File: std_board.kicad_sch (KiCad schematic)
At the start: 208 parts, among them IC1 ESP32, IC2 ACS712, IC4 AMS1117-V, J1 Jumper, J10 J_DHT11, J11 Jumper, J12 Jumper, J14 Jumper, J15 Jumper, J16 J_PRess, J17 Jumper, J18 Jumper, J19 Jumper, J2 Jumper, J20 Jumper, J21 Jumper, J22 Jumper, J23 Jumper, J24 Jumper, J25 Jumper, J26 Jumper, J3 Jumper, J31 Jumper, J32 Jumper, J33 Jumper, J34 Jumper, J35 Jumper, J36 Jumper, J37 Jumper, J38 Jumper, J39 Jumper, J4 Jumper, J40 Jumper, J41 Jumper, J42 Jumper, J43 Jumper, J44 Jumper, J45 Jumper, J5 Jumper, J6 Jumper, J9 Jumper, T1 TRIAC_Micro, T10 TRIAC_Micro, T2 TRIAC_Micro, T3 TRIAC_Micro, T4 NPN_MMBT222A, T5 NPN_MMBT222A, T6 NPN_MMBT222A, T7 NPN_MMBT222A, T8 PNP_2N3906, T9 NPN_MMBT222A, U1 LNK306, U3 L7805CV

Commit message: board update some documentation of pinout link with description
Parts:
- removed C22: 2.2 uF, thmalmeida:C3_elec_5x4.5_pth, symbol std_board-rescue:CP_Micro-thmalmeida
- removed C23: 22 uF, thmalmeida:C3_elec_5x4.5_pth, symbol std_board-rescue:CP_Micro-thmalmeida
- removed IC4: AMS1117-V, Package_TO_SOT_SMD:SOT-223, symbol std_board-rescue:AMS1117-V-thmalmeida
- removed J35: Jumper, thmalmeida:J_0603, symbol std_board-rescue:Jumper-thmalmeida
- added C22: 47 nF, Capacitor_SMD:C_0805_2012Metric, symbol std_board-rescue:C_Micro-RESCUE-[GenericBoard]_standard_pcb-[GenericBoard]-stan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
- added R72: 56 k, Resistor_SMD:R_0805_2012Metric, symbol std_board-rescue:R_Micro-thmalmeida
- added R77, R78: 330, Resistor_SMD:R_0805_2012Metric, symbol std_board-rescue:R_Micro-thmalmeida
- J38: Spice_Model Jumper -> (none); Spice_Netlist_Enabled Y -> (none); Spice_Primitive X -> (none)
- Opto4: footprint Housings_DIP:DIP-6_W7.62mm -> Package_DIP:DIP-6_W7.62mm
- R45: value 180 k -> 39 k
- R46, R48: value 120 -> 3.3 k
- R47: value 180 k -> 56 k
- R60: value 120 k -> 39 k
- T1: footprint thmalmeida:TO-220_thm -> Package_TO_SOT_THT:TO-220-3_Vertical
- T3: footprint TO_SOT_Packages_THT:TO-220_Neutral123_Vertical -> Package_TO_SOT_THT:TO-220-3_Vertical
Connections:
- net +3.3V: now also R72.1 (A)
- net +5V: now also J42.1 (A), U3.1 (IN)
- net GND: now also C22.2 (B)
- net Power_AC_R: no longer R70.1 (A), R71.1 (A), T10.2 (A)
- net Power_AC_T: now also R70.1 (A), R71.1 (A), T10.2 (A)
- net iSensor1: now also R77.1 (A)
- net iSensor2: now also R78.1 (A)
- net at C19.1 (A), LS1.2 (B), R46.2 (B)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: now also R77.2 (B)
- net at C20.1 (A), LS2.2 (B), R48.2 (B)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: now also R78.2 (B)
- new net K0_in: C22.1 (A), R72.2 (B)
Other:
- moved on the sheet: C10, C11, C19, C20, C8, C9, F1, Inputs1, J23, J34, J36, J37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

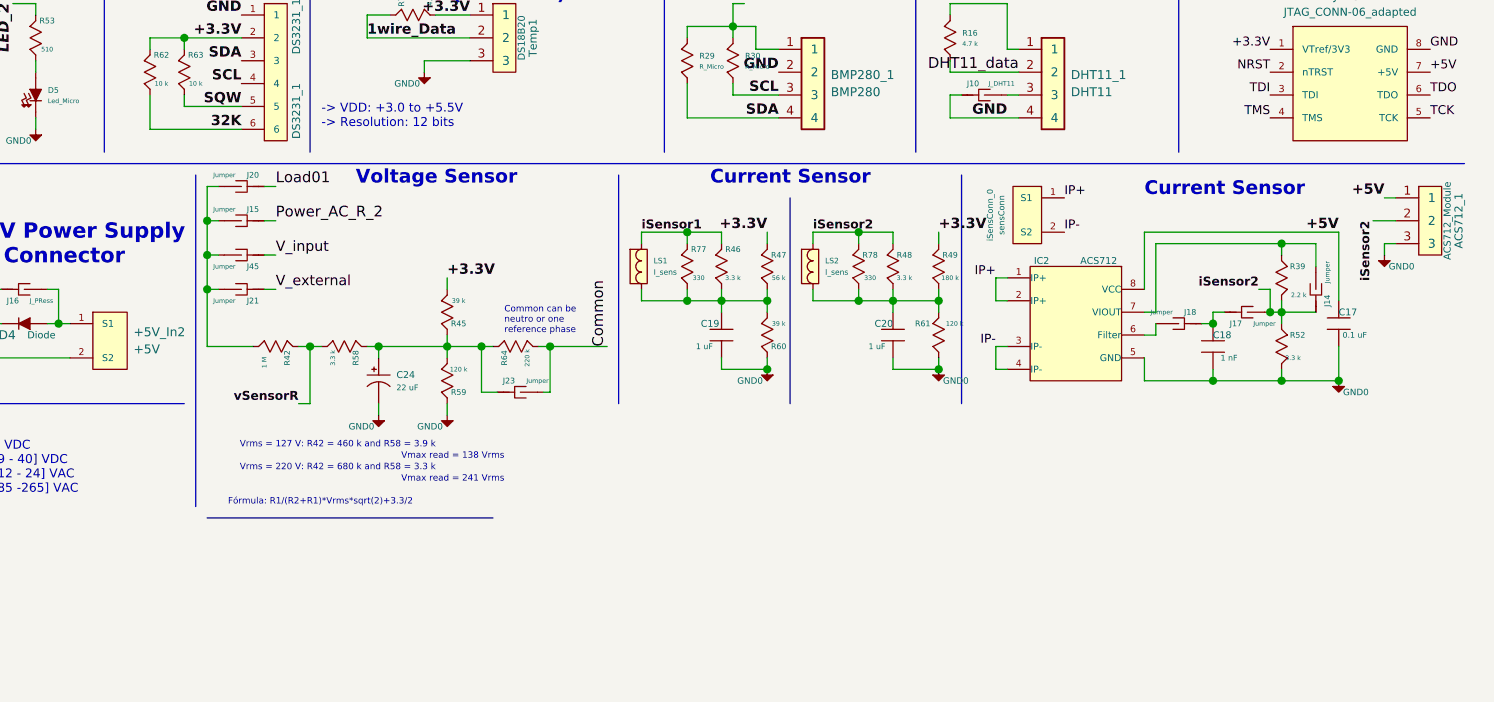
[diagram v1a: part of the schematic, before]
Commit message: current sensor 1 added resistors for voltage divider
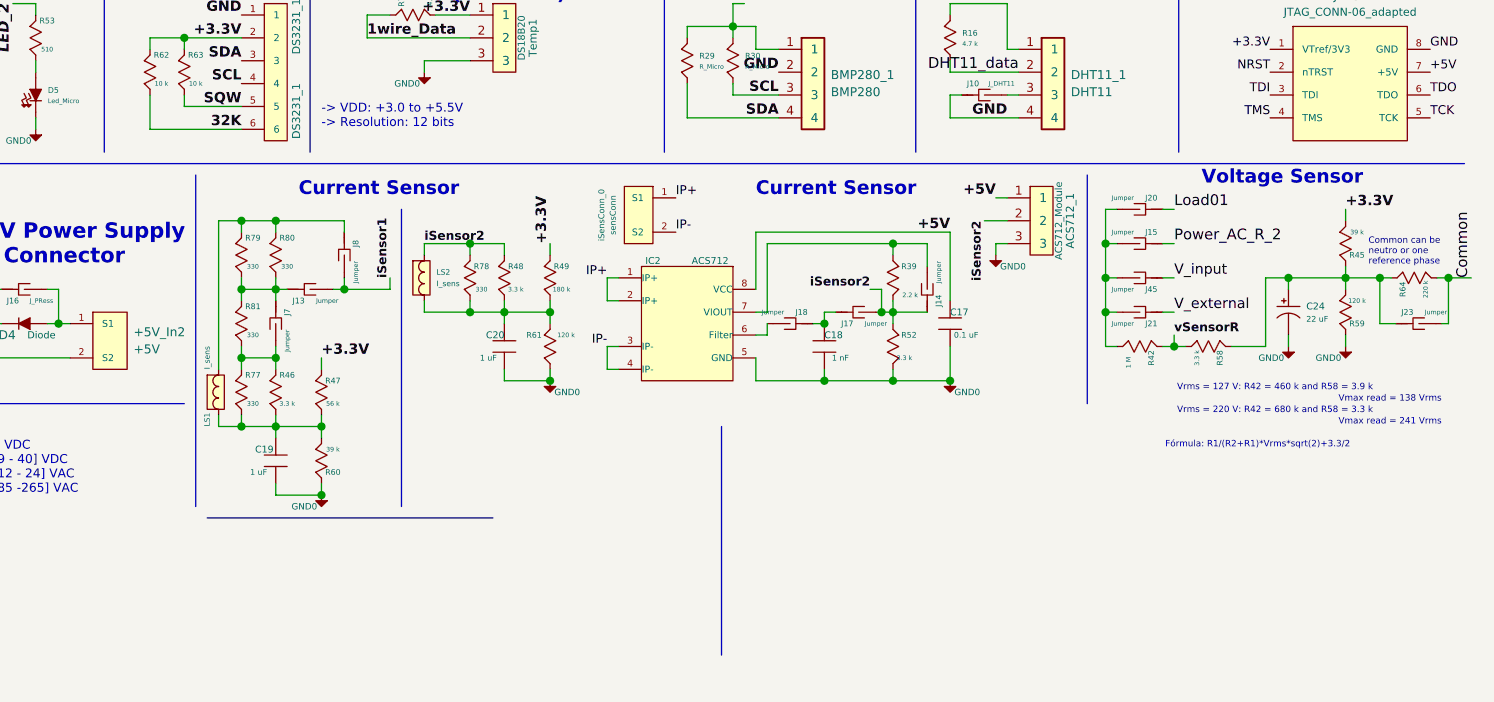
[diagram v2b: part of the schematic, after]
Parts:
- added J13, J7, J8: Jumper, thmalmeida:J_0603, symbol std_board-rescue:Jumper-thmalmeida
- added R79, R80, R81: 330, Resistor_SMD:R_0805_2012Metric, symbol std_board-rescue:R_Micro-thmalmeida
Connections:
- net iSensor1: now also J13.2 (B), J8.2 (B); no longer LS1.1 (A), R46.1 (A), R77.1 (A)
- new net: J7.2 (B), R46.1 (A), R77.1 (A), R81.2 (B)
- new net: J8.1 (A), LS1.1 (A), R79.1 (A), R80.1 (A)
- new net: J13.1 (A), J7.1 (A), R79.2 (B), R80.2 (B), R81.1 (A)
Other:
- moved on the sheet: ACS712_1, C17, C18, C19, C20, C24, IC2, J14, J15, J17, J18, J20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

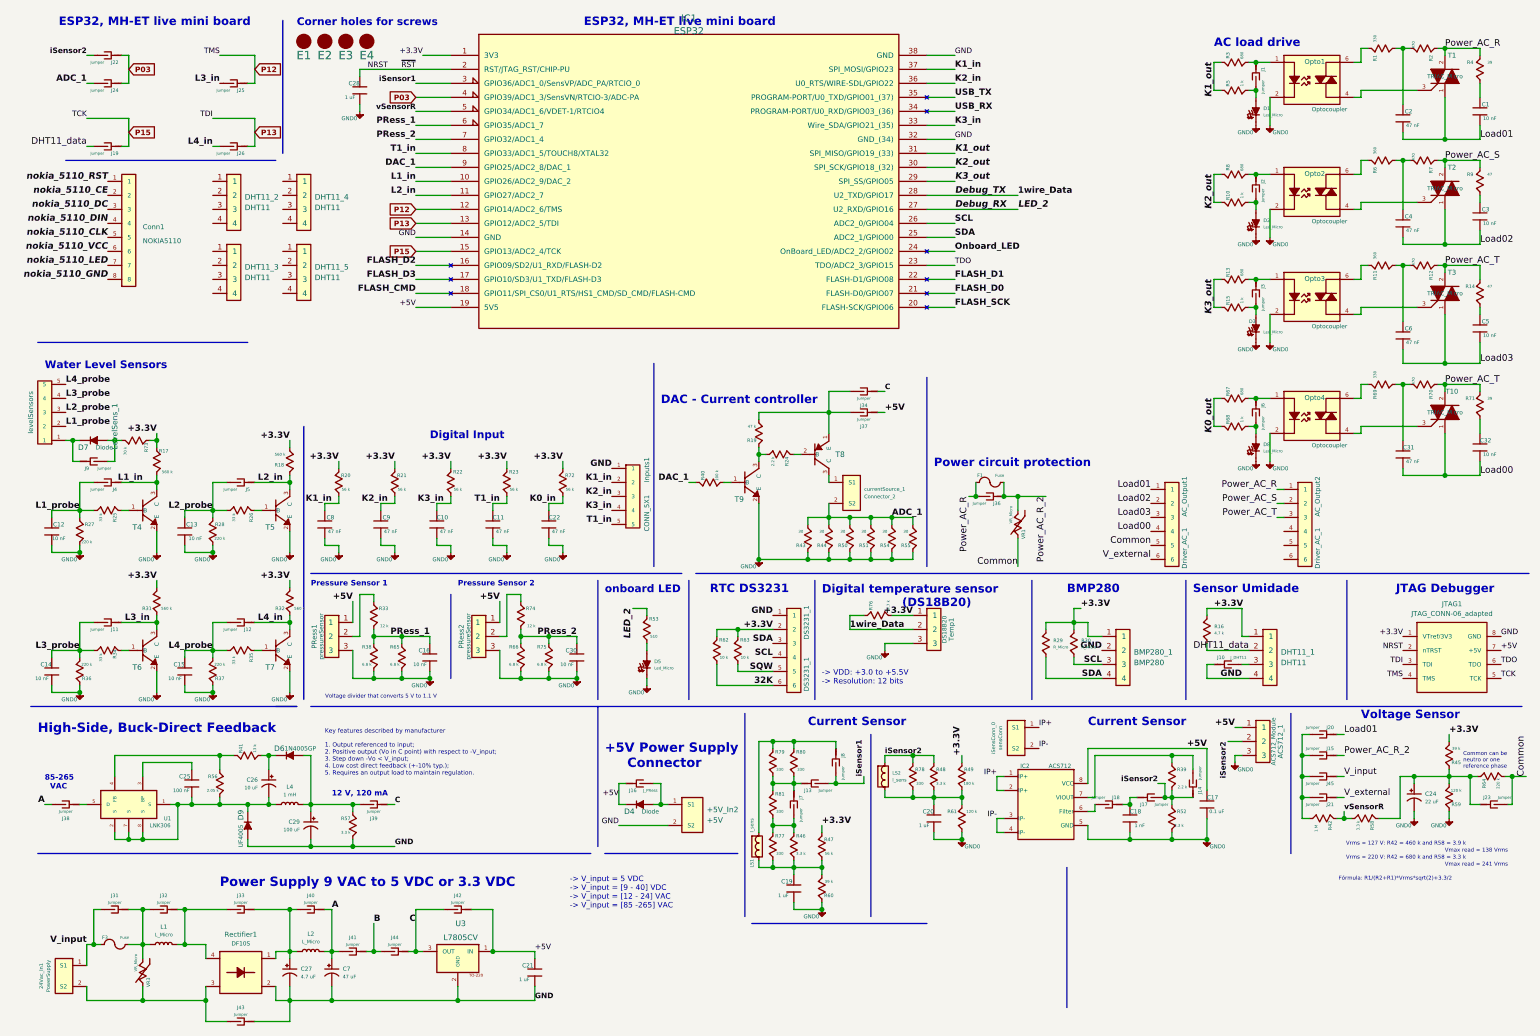
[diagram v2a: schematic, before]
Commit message: changed pi filter values at input of power supply
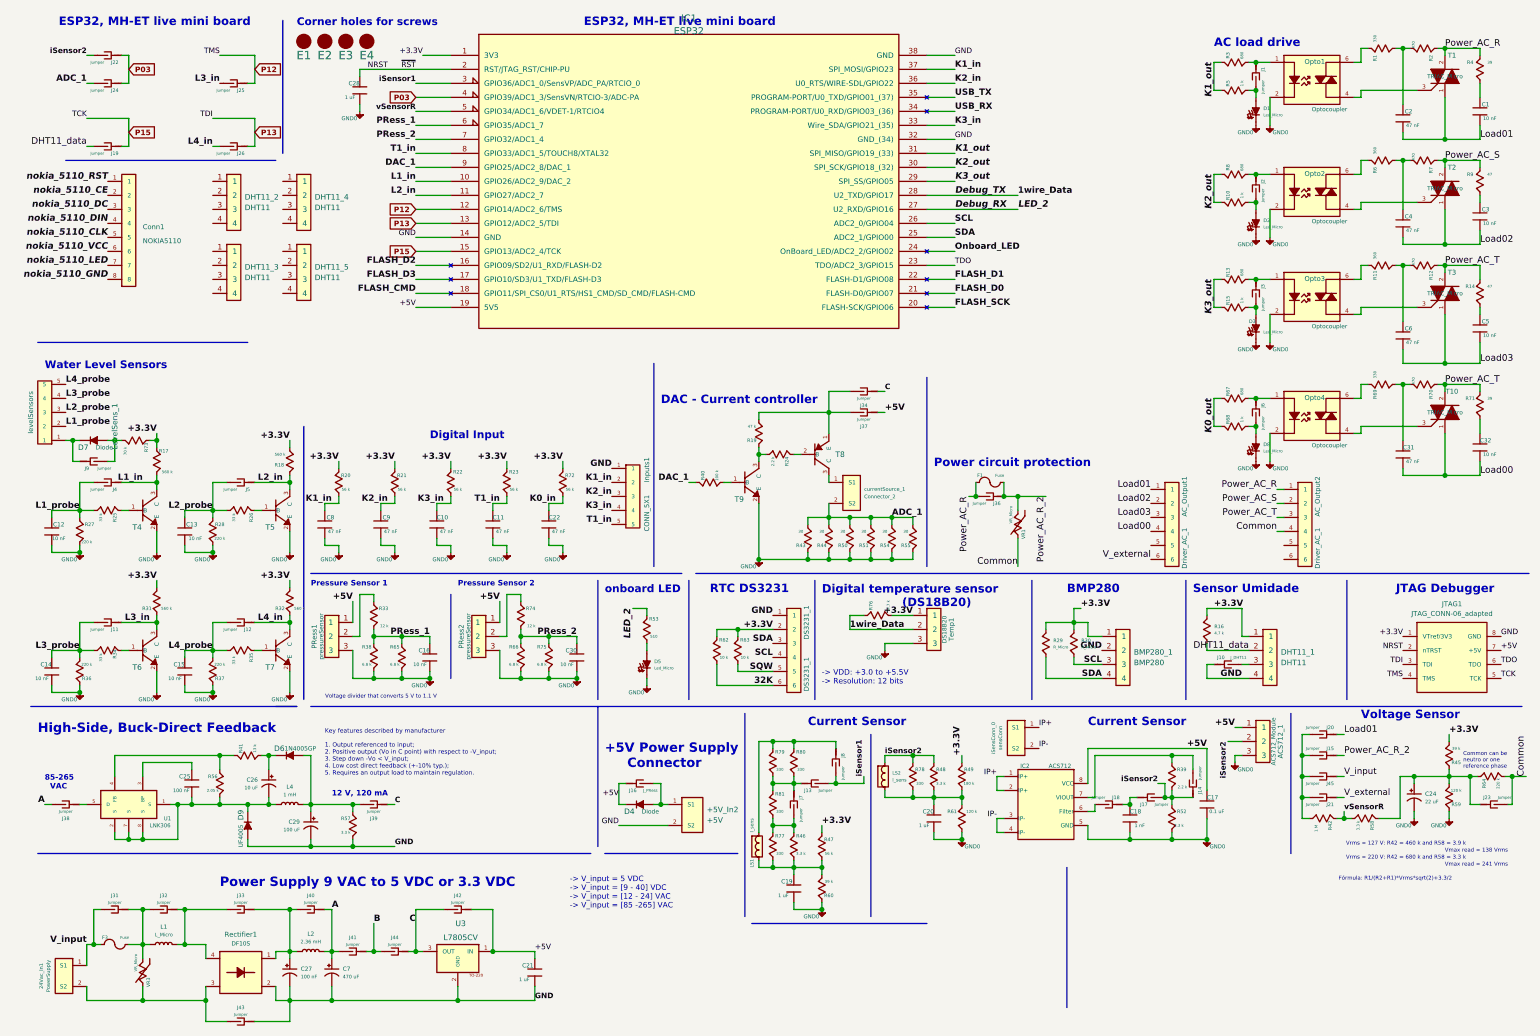
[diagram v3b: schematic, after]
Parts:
- C27: value 4.7 uF -> 100 nF; Rated Voltage [V] vv -> 400 V
- C7: value 47 uF -> 470 uF; Rated Voltage [V] vv -> 50 V
- L2: value L_Micro -> 2.36 mH
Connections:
- net Common: now also AC_Output2.4; no longer AC_Output1.5
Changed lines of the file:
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@@
     (stroke (width 0) (type default))
   )
+  (wire (pts (xy 238.76 106.68) (xy 240.03 106.68))
+    (stroke (width 0) (type default))
+  )
   (wire (pts (xy 270.002 151.13) (xy 273.812 151.13))
     (stroke (width 0) (type default))
@@
     (effects (font (size 0.9906 0.9906) (thickness 0.1981) bold) (justify left bottom))
   )
-  (label "Common" (at 215.9 109.22 180) (fields_autoplaced)
+  (label "Common" (at 238.76 106.68 180) (fields_autoplaced)
     (effects (font (size 1.1938 1.1938)) (justify right bottom))
   )
@@
       (effects (font (size 0.762 0.762)))
     )
-    (property "Value" "L_Micro" (at 63.5 181.102 90)
+    (property "Value" "2.36 mH" (at 63.5 181.102 90)
       (effects (font (size 0.635 0.635)))
     )
@@
       (effects (font (size 0.762 0.762)) (justify left))
     )
-    (property "Value" "47 uF" (at 69.2912 187.452 0)
+    (property "Value" "470 uF" (at 69.2912 187.452 0)
       (effects (font (size 0.635 0.635)) (justify left))
     )
@@
       (effects (font (size 1.524 1.524)))
     )
-    (property "Rated Voltage [V]" "vv" (at 76.2 189.23 0)
+    (property "Rated Voltage [V]" "50 V" (at 76.2 189.23 0)
       (effects (font (size 1.524 1.524)) hide)
     )
@@
       (effects (font (size 0.762 0.762)) (justify left))
     )
-    (property "Value" "4.7 uF" (at 61.6712 187.452 0)
+    (property "Value" "100 nF" (at 61.6712 187.452 0)
       (effects (font (size 0.635 0.635)) (justify left))
     )
@@
       (effects (font (size 1.524 1.524)))
     )
-    (property "Rated Voltage [V]" "vv" (at 68.58 189.23 0)
+    (property "Rated Voltage [V]" "400 V" (at 68.58 189.23 0)
       (effects (font (size 1.524 1.524)) hide)
     )
